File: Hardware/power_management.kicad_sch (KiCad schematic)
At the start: 37 parts, among them J2 Conn_01x03, SW27 SW_DPDT_x2, U2 BQ24040, U3 BQ51050BRHL, U4 AP22814BW5, U5 AP7333

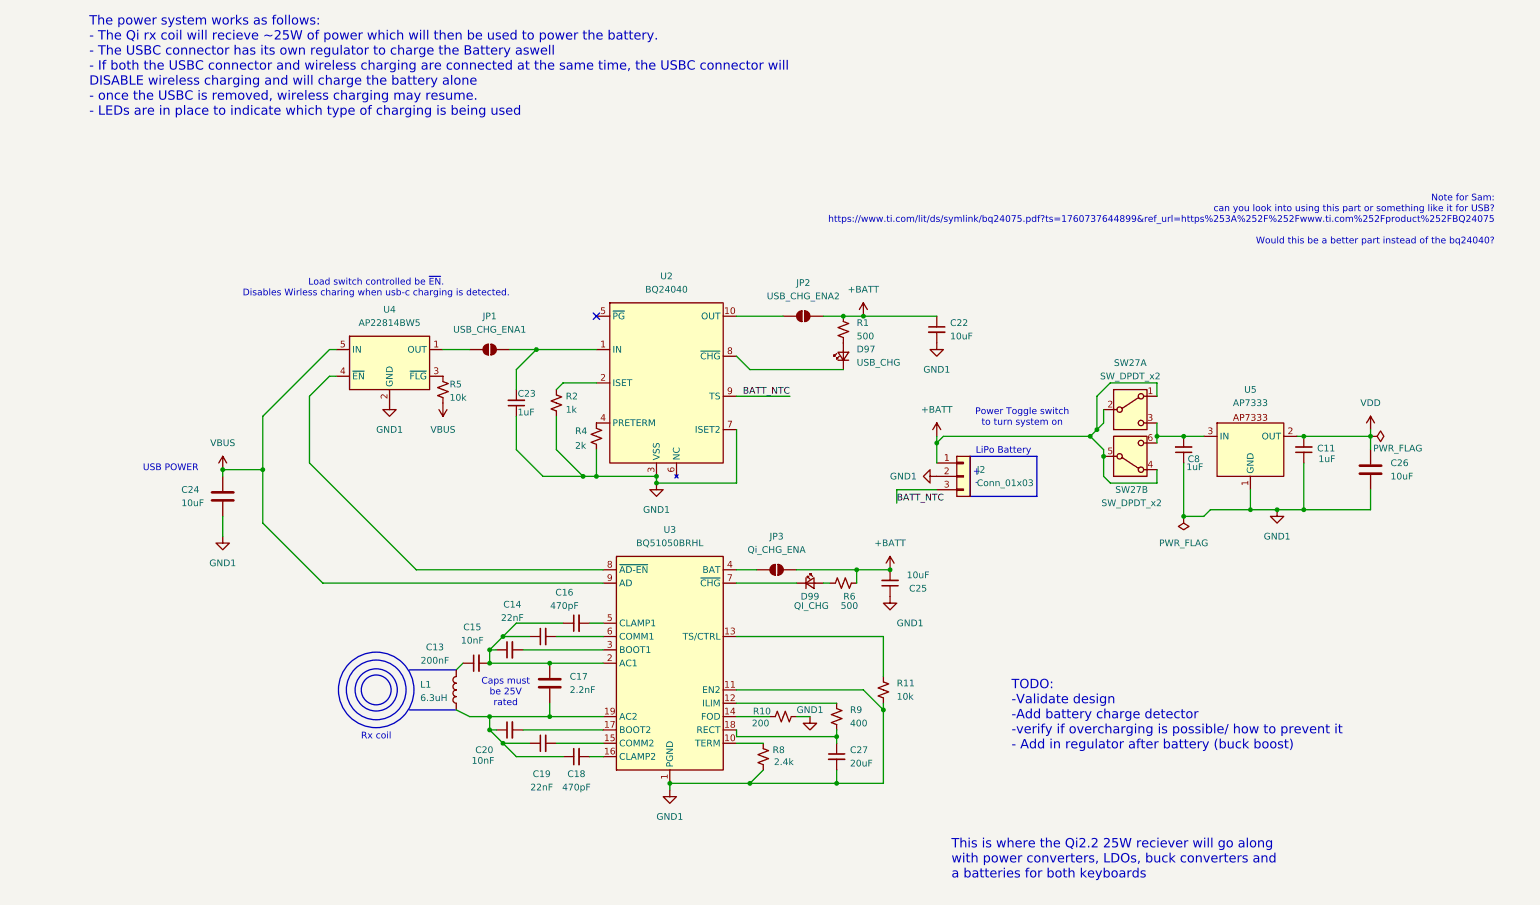
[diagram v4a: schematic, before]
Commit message: Refactor keyboard and power schematics, remove backups
Deleted old hornet_kb schematic backup ZIPs. Updated hornet_kb.kicad_sch: reorganized right-hand row/column labels and wires for physical pin convenience, added annotation, and removed redundant global labels. In power_management.kicad_sch: removed decorative Rx coil circles, updated annotation positions and text, and shifted many schematic elements for improved clarity and layout.
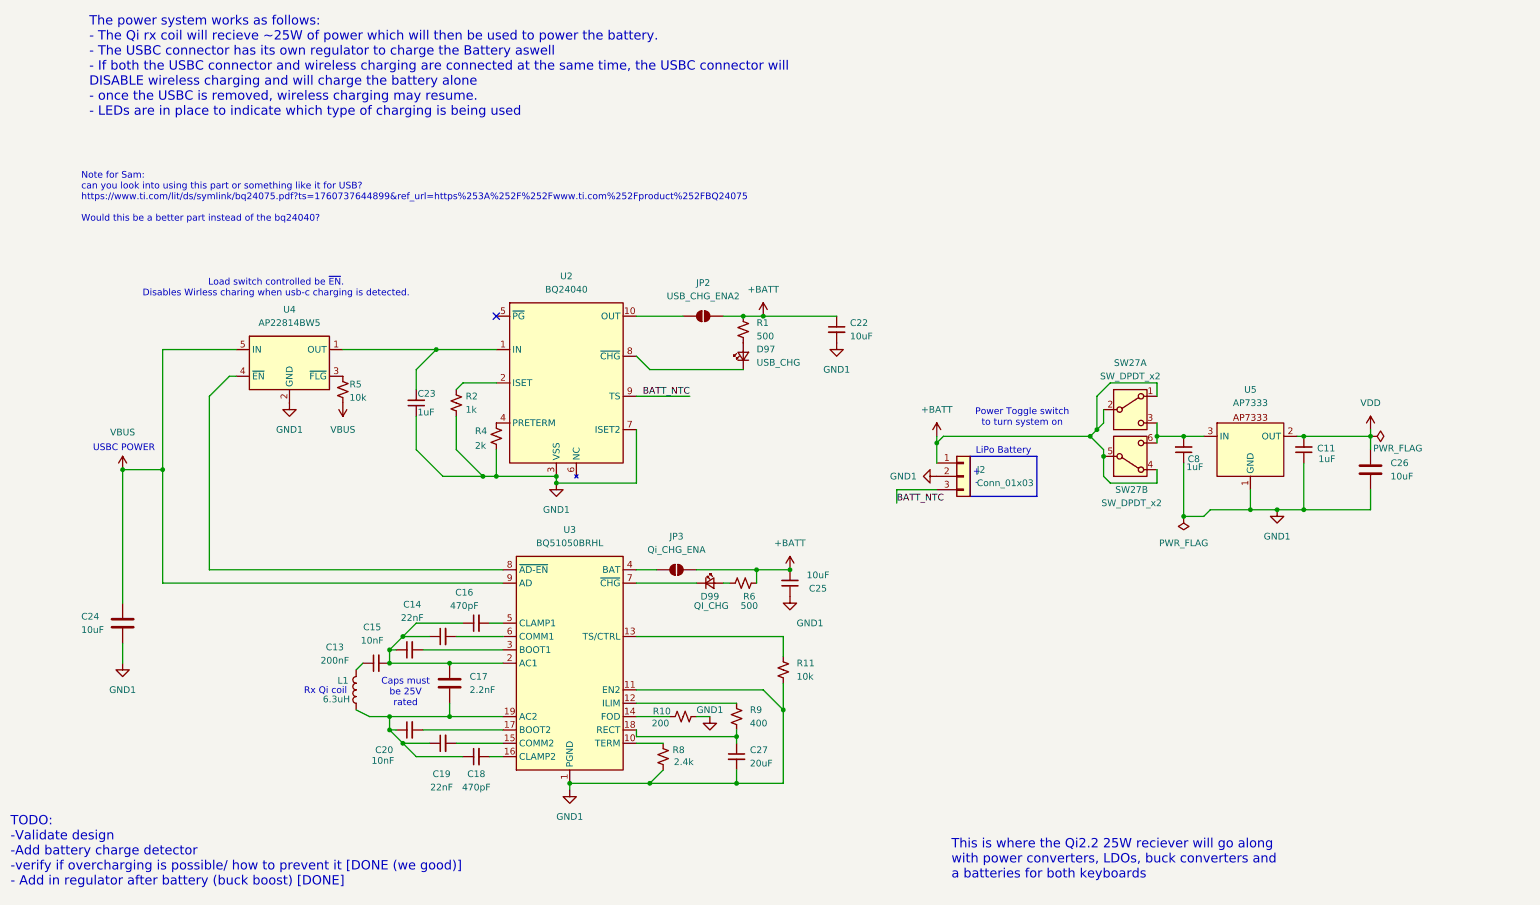
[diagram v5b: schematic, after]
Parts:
- removed JP1: USB_CHG_ENA1, Jumper:SolderJumper-2_P1.3mm_Open_TrianglePad1.0x1.5mm, symbol Jumper:SolderJumper_2_Open
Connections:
- net at C23.2, U2.1 (IN): now also U4.1 (OUT)
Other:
- note added: "Rx Qi coil"
- note added: "TODO: -Validate design -Add battery charge detector -verify if overcharging is possible/ how to prevent it [DONE (we good)] - Add in regulator after battery (buck boost) [DONE]"
- note added: "USBC POWER"
- note removed: "Rx coil"
- note removed: "TODO: -Validate design -Add battery charge detector -verify if overcharging is possible/ how to prevent it - Add in regulator after battery (buck boost)"
- note removed: "USB POWER"
- moved on the sheet: C13, C14, C15, C16, C17, C18, C19, C20, C22, C23, C24, C25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

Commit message: Update schematic coordinates and add notes
Adjusted coordinates for wires, junctions, and no_connects in hornet_kb.kicad_sch for improved layout clarity. Added company info and new design notes. Deleted outdated backup ZIP file.
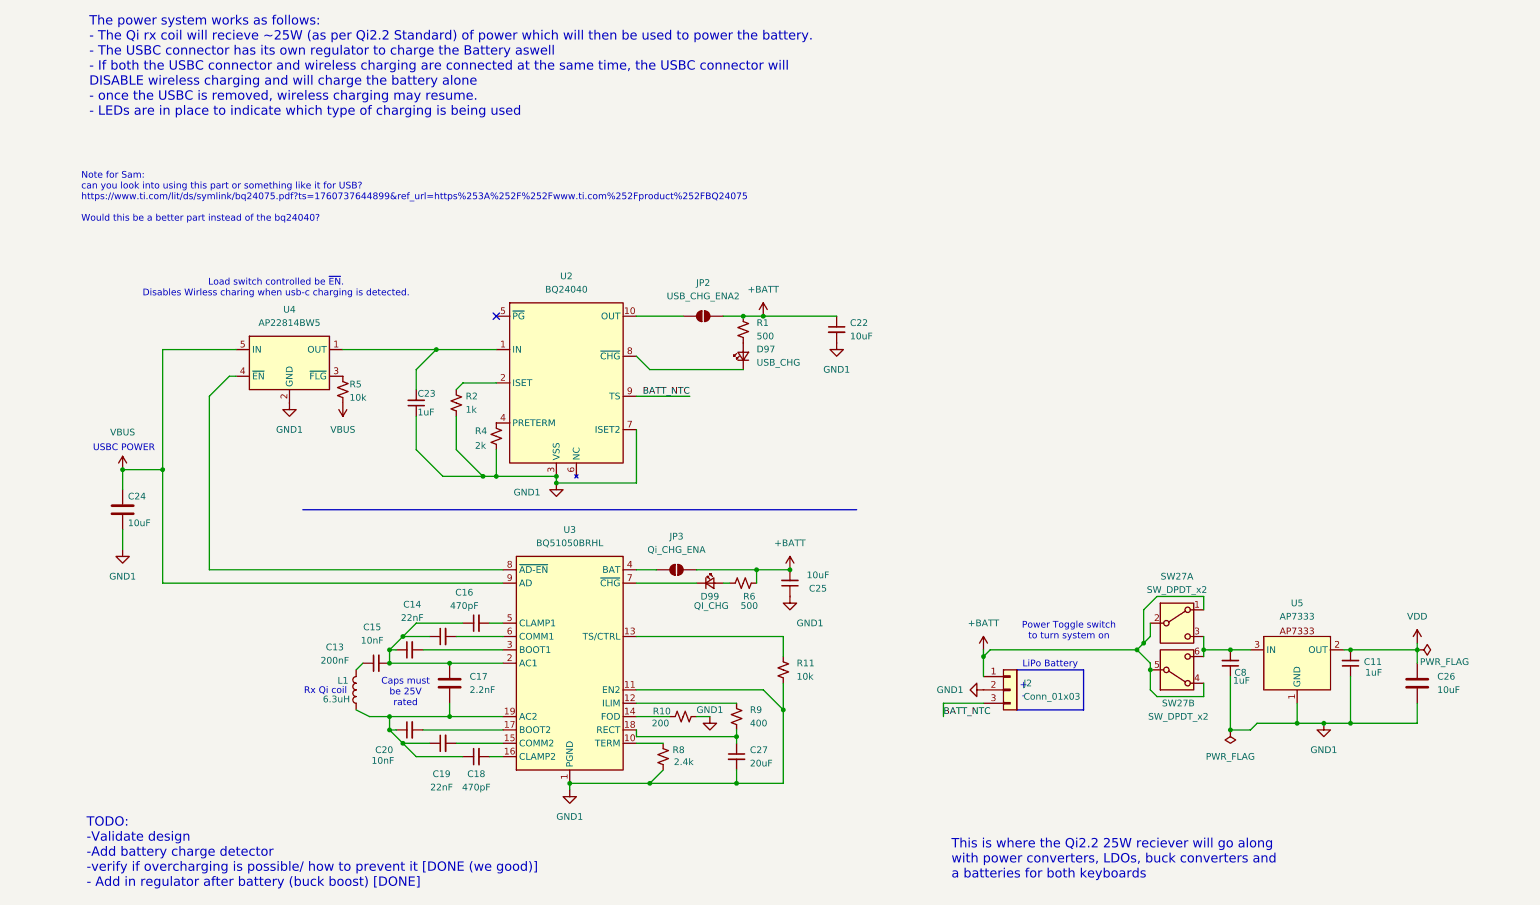
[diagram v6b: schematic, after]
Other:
- note added: "The power system works as follows: - The Qi rx coil will recieve ~25W (as per Qi2.2 Standard) of power which will then be used to power the battery. - The USBC connector has its own regulator to charge the Battery aswell - If both the USBC connector and wireless charging are connected at the same time, the USBC connector will DISABLE wireless charging and will charge the battery alone - once the 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"
- note removed: "The power system works as follows: - The Qi rx coil will recieve ~25W of power which will then be used to power the battery. - The USBC connector has its own regulator to charge the Battery aswell - If both the USBC connector and wireless charging are connected at the same time, the USBC connector will DISABLE wireless charging and will charge the battery alone - once the USBC is removed, wireles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"
- moved on the sheet: C11, C24, C26, C8, J2, SW27A, SW27B, U5

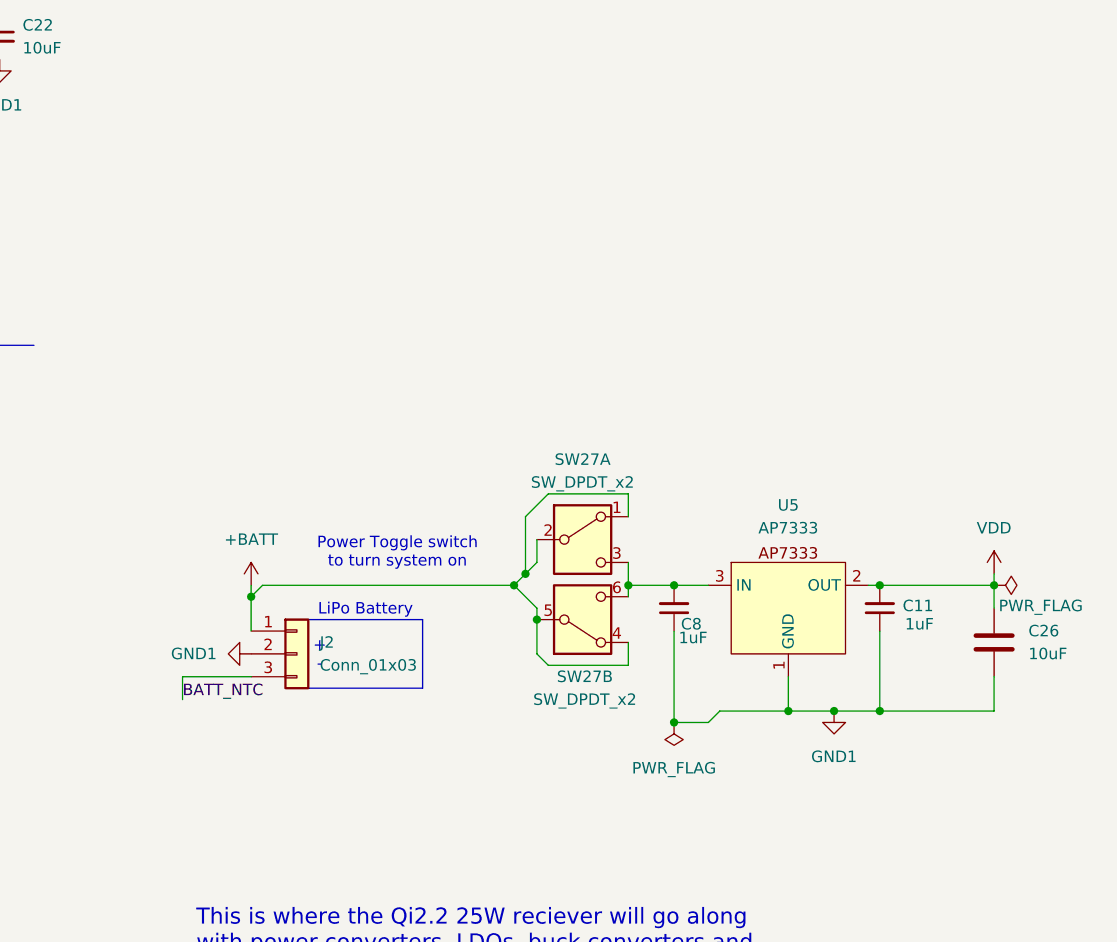
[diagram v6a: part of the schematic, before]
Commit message: Update schematic for rotary encoder and matrix layout
Added new symbols and labels for rotary encoder connections, updated wire routing and junctions, and adjusted matrix row/column positions for improved clarity and alignment. Also corrected text annotations to better describe left and right hand keyboard sections.
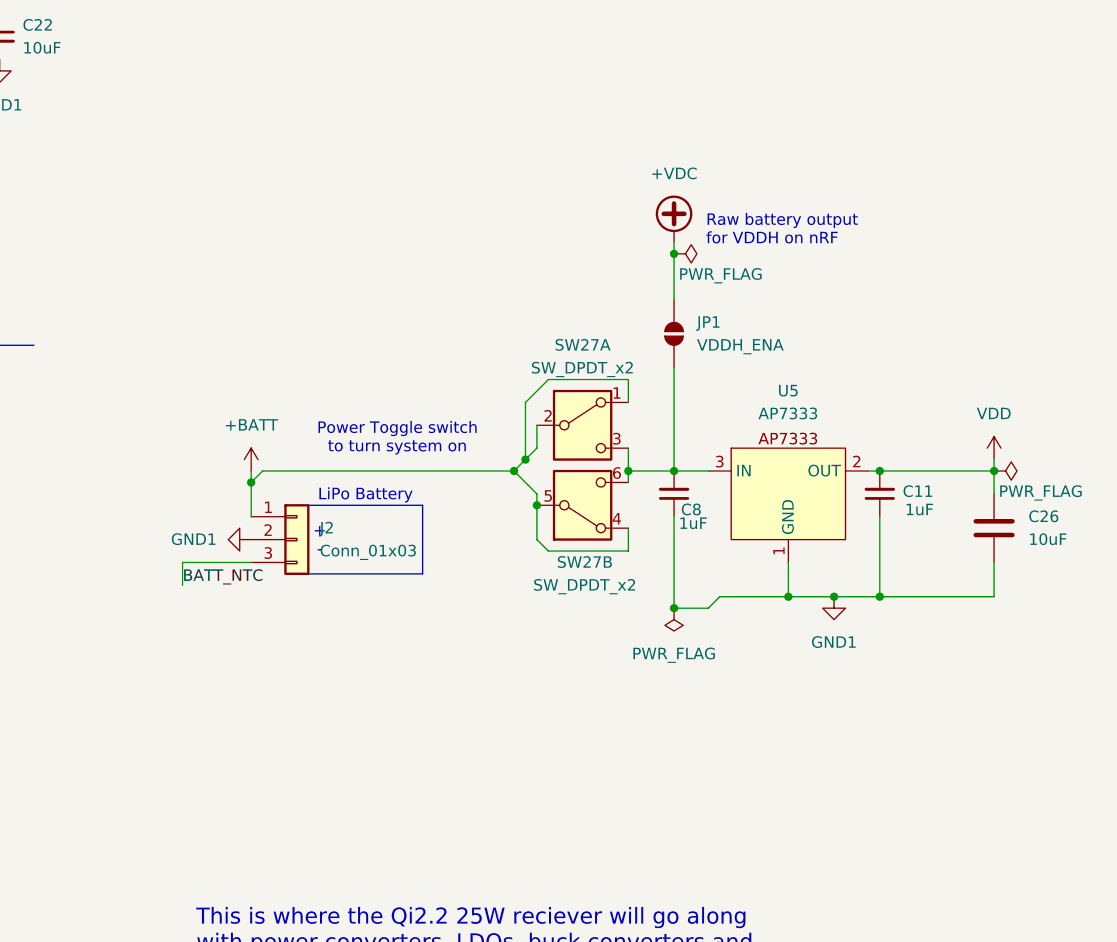
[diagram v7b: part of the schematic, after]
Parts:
- added JP1: VDDH_ENA, Jumper:SolderJumper-2_P1.3mm_Open_TrianglePad1.0x1.5mm, symbol Jumper:SolderJumper_2_Open
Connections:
- net at C8.2, SW27.3 (C), SW27.6 (C)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: now also JP1.1 (A)
- new net +VDC: JP1.2 (B)
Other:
- note added: "Raw battery output for VDDH on nRF"
- moved on the sheet: C11, C26, C8, J2, SW27A, SW27B, U5

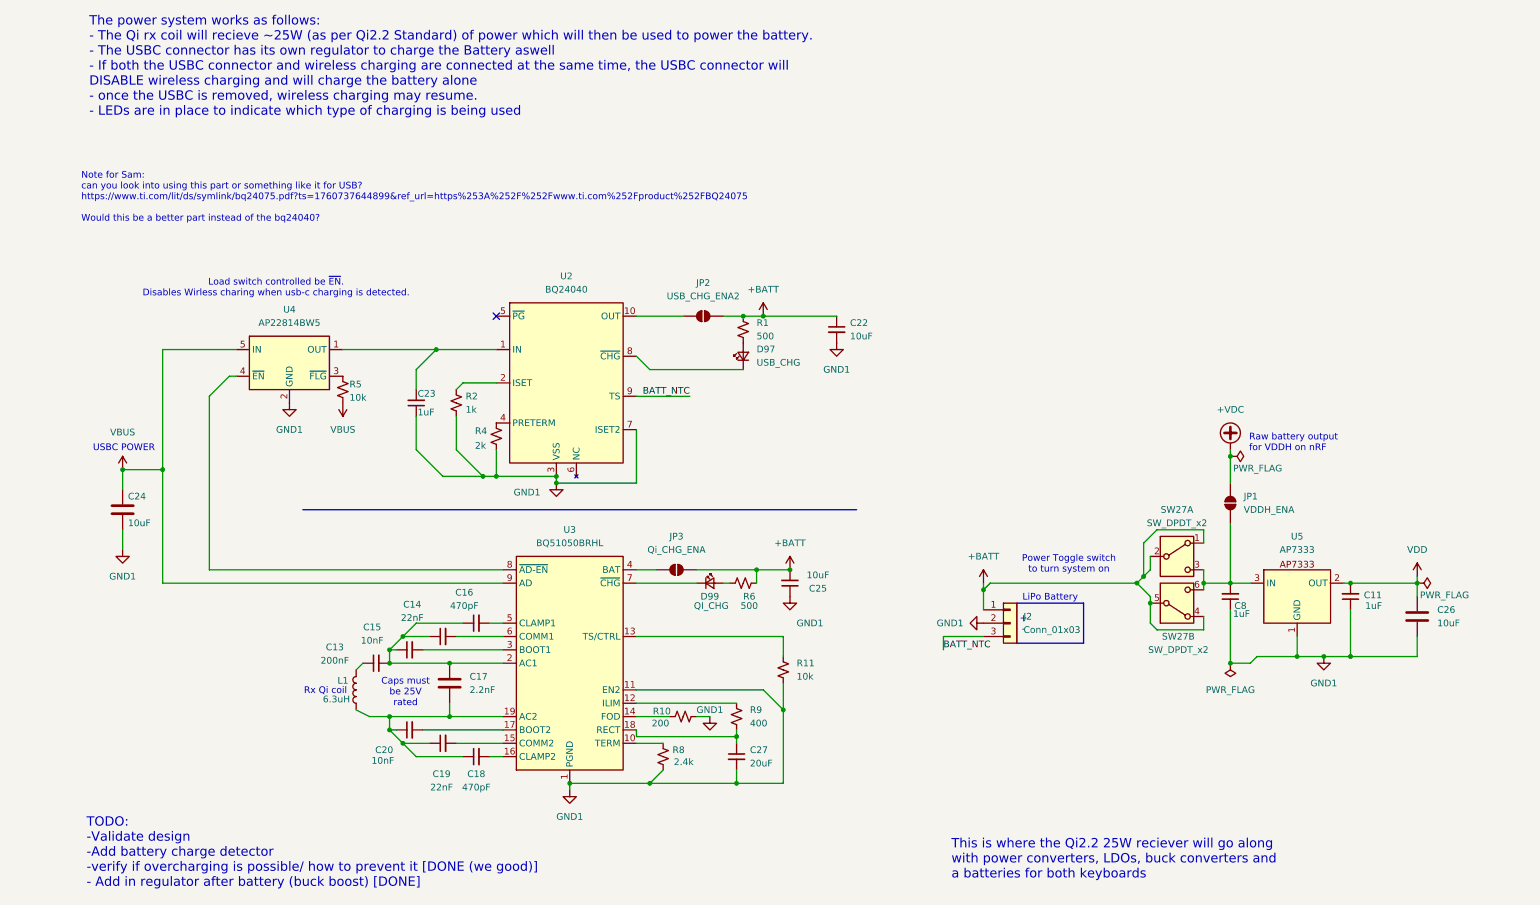
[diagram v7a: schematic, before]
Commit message: Add antenna symbol and update schematic connections
Introduced a new Device:Antenna symbol to the hornet_kb schematic and added its instance. Updated various wire and junction connections, including changes to VBUS, GND, and capacitor placements. Replaced GND1 symbols with GND in power_management schematic for consistency. Adjusted text annotations and wire routing in all affected schematics to reflect new connections and improve clarity.
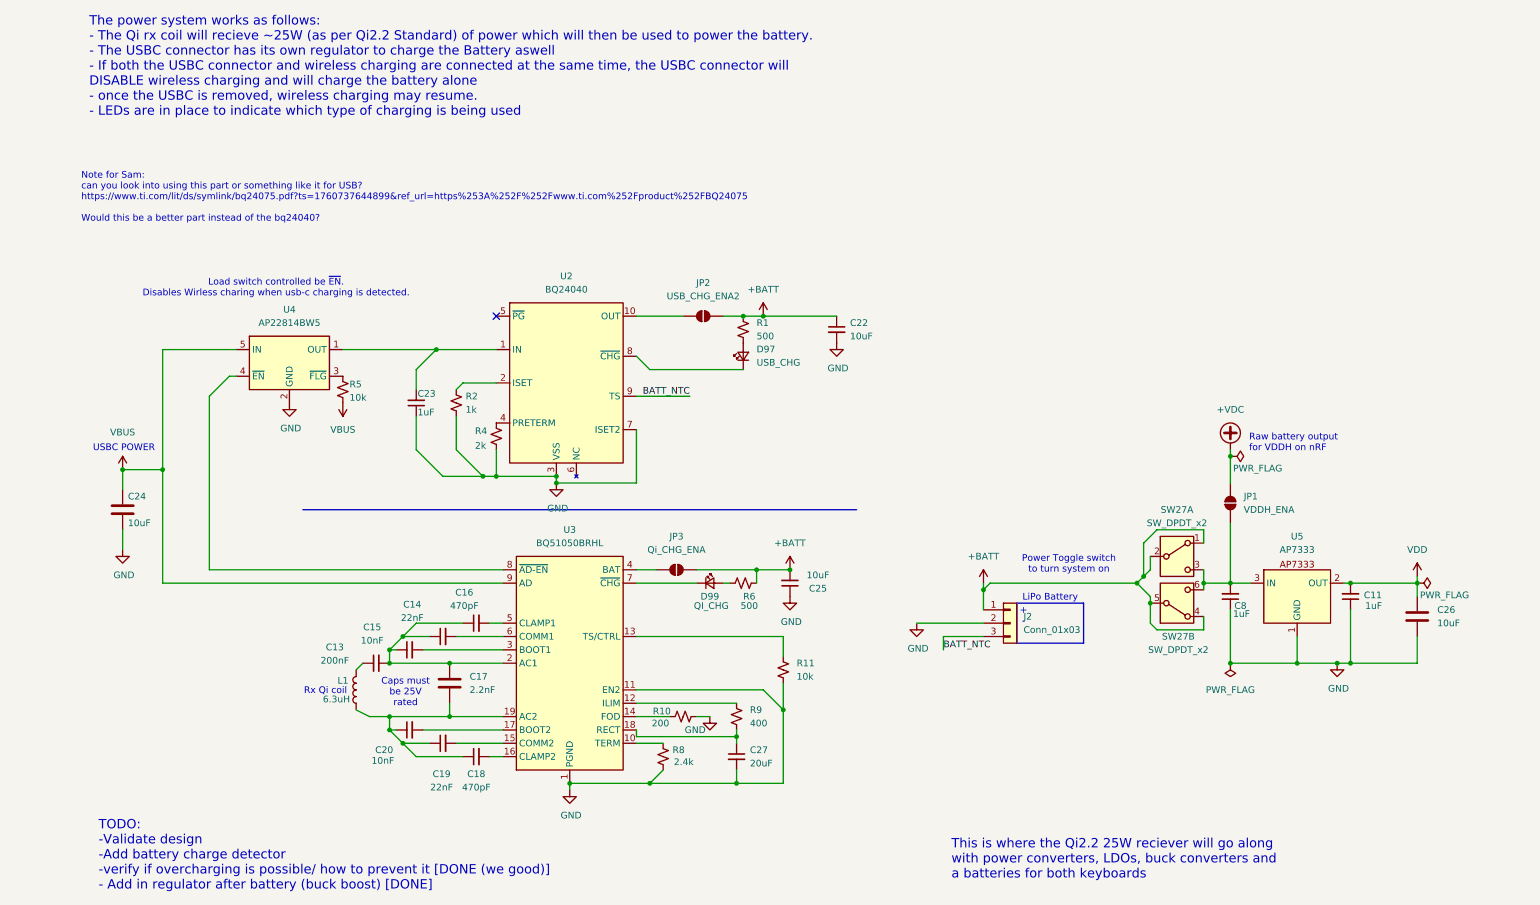
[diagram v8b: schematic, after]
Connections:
- net GND1 renamed GND
